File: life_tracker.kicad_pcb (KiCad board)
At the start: 2 copper layers, 52 x 78 mm, 16 parts, among them J1 TACTILE-NAV-SWITCH, U1 WeMos_D1_mini, U2 I2C_128x64_OLED, U3 AS1115-BSST, U4 PTS526-tactile-button, U5 PTS526-tactile-button

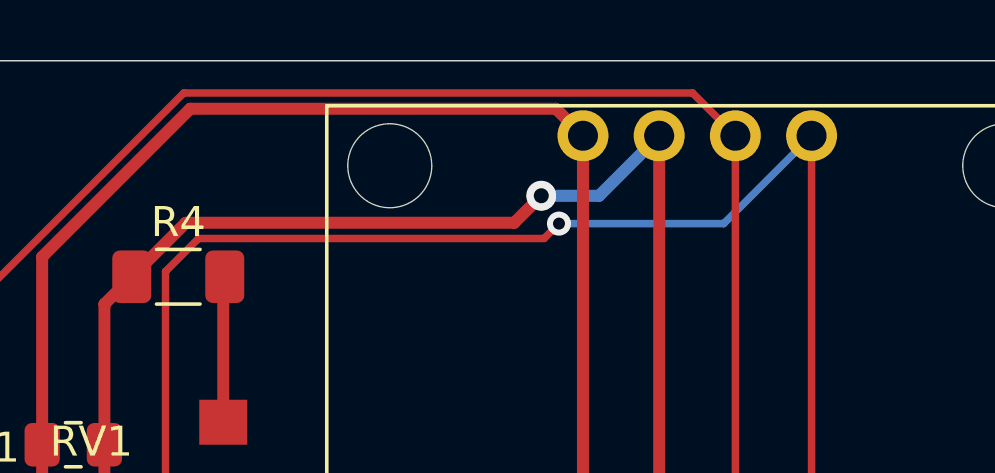
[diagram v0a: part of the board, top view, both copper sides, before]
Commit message: Fix swapped I2C connection.
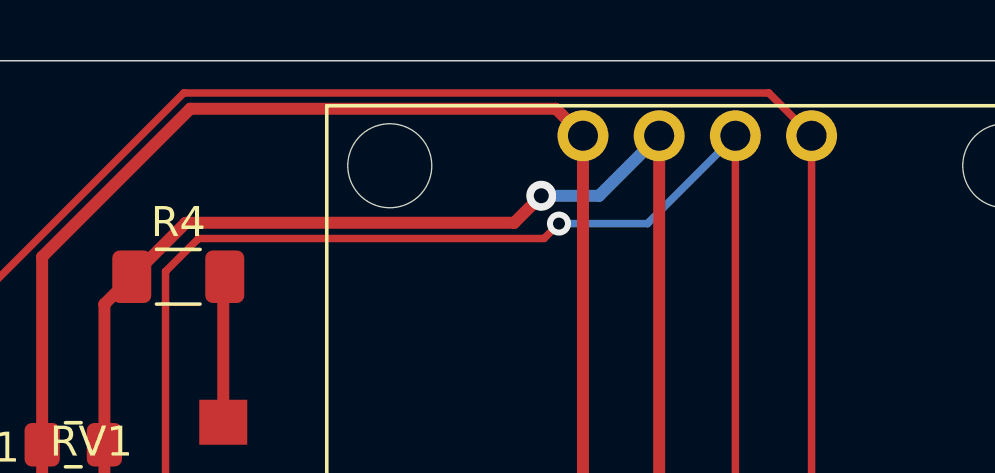
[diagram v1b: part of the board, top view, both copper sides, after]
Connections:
- U1 pad 10: GND -> Net-(U1-Pad10)
- U3 pad 1: Net-(R1-Pad2) -> Net-(R2-Pad2)
- U3 pad 14: Net-(R2-Pad2) -> Net-(R1-Pad2)
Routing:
- net Net-(R2-Pad2): track 156.2 -> 149.7 mm, vias 4 -> 1
- net Net-(R1-Pad2): track 144.9 -> 151.5 mm, vias 1 -> 4

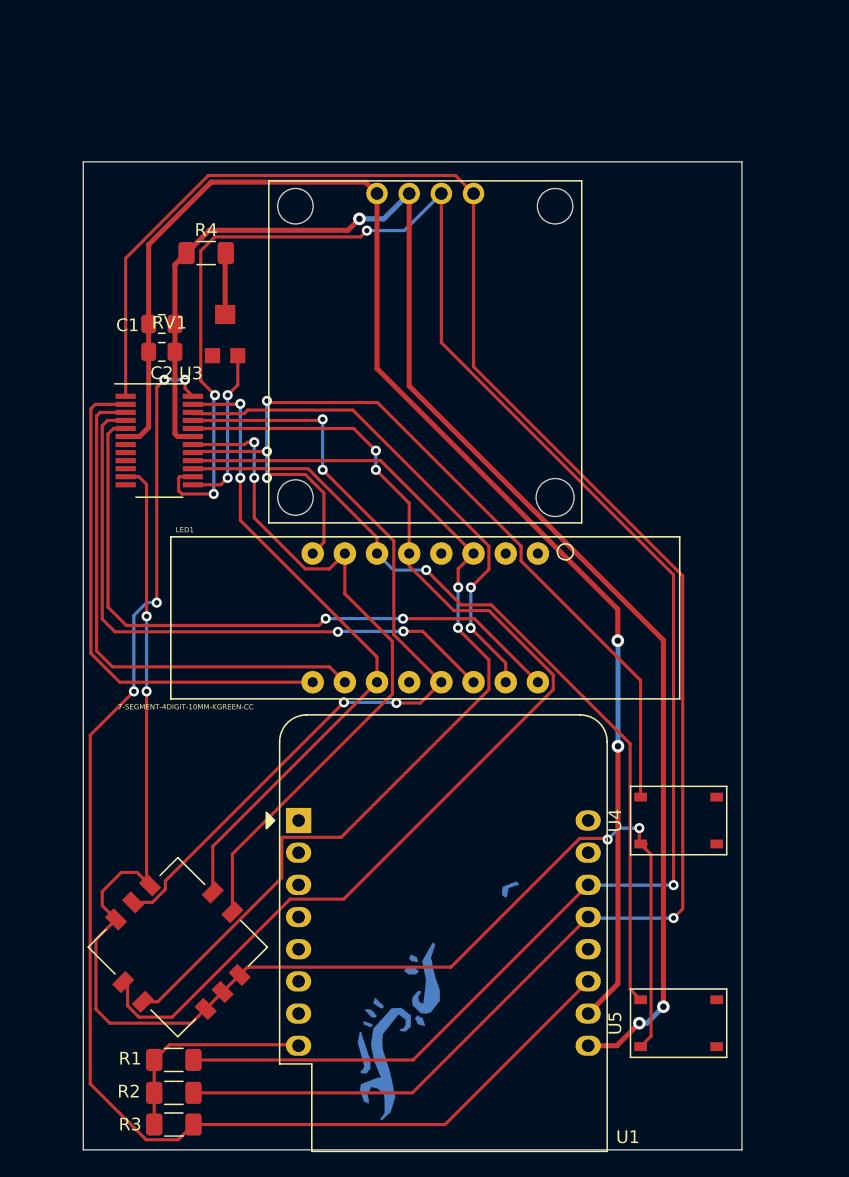
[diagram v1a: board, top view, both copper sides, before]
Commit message: Added footprints for new buttons and redid layout for bigger board, and OLED on top of D1.
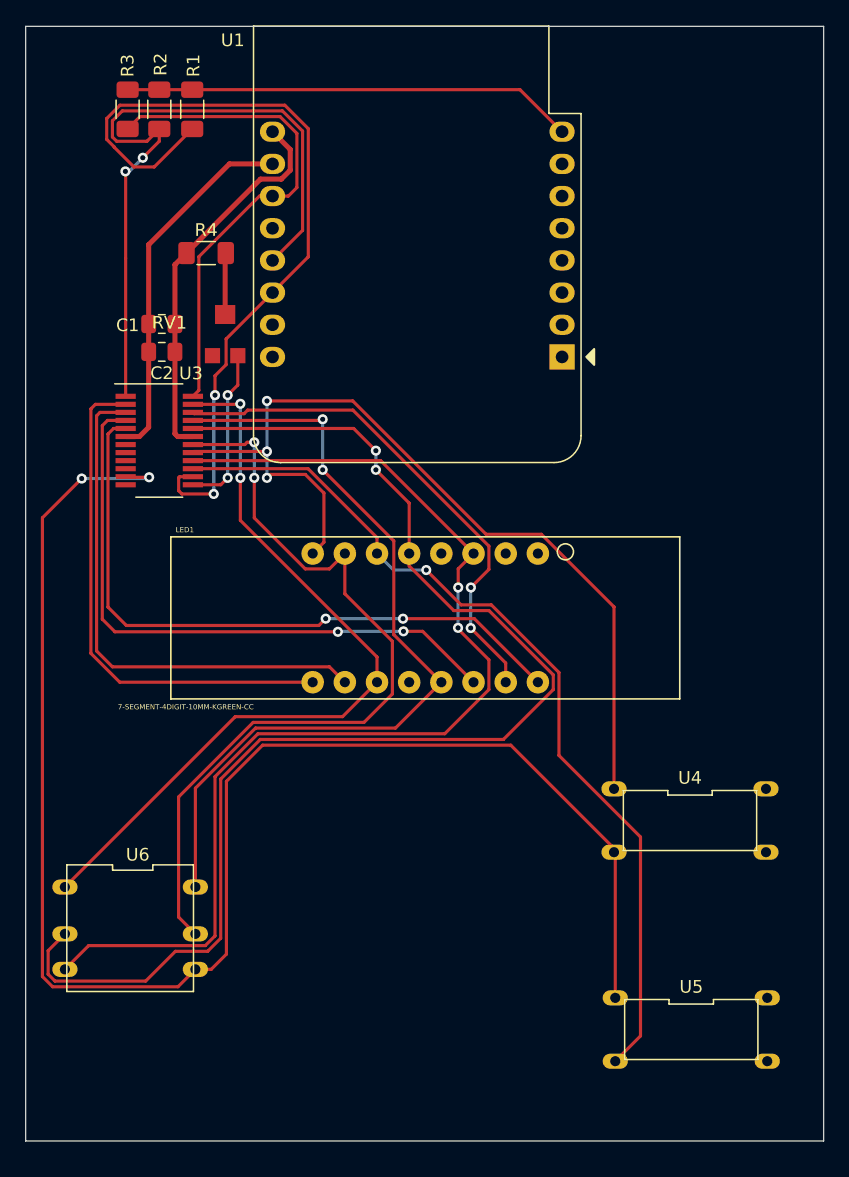
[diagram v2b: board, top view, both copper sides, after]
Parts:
- removed J1: TACTILE-NAV-SWITCH, MyFootprints:JS1300AQ
- removed U2: I2C_128x64_OLED, MyFootprints:I2C_128x64_OLED
- removed svg2mod: G***, MyFootprints:squirrel2
- removed svg2mod: G***, MyFootprints:plains_walker
- added U6: TACTILE-NAV-STICK-DIP, MyFootprints:TACTILE-NAV-STICK-DIP, F.Cu at (103.7, 110.5)
- U4, U5: footprint MyFootprints:pts526-tactile-button -> MyFootprints:TACTILE-DIP-BUTTON
- moved R3 80.2 mm to (103.5, 45.9), turned to 270 degrees
- moved R2 77.7 mm to (106.0, 45.9), turned to 270 degrees
- moved R1 75.1 mm to (108.6, 45.9), turned to 270 degrees
- moved U1 42.1 mm to (137.8, 65.4), turned to 180 degrees
- moved U5 1.12 mm to (148.0, 118.5), turned to 270 degrees
- moved U4 0.90 mm to (147.9, 102.0), turned to 270 degrees
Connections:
- U1 pad 10: Net-(U1-Pad10) -> GND
- U3 pad 11: Net-(J1-Pad10) -> Net-(U3-Pad11)
- U4 pad 3: Net-(J1-Pad10) -> Net-(U3-Pad11)
- U5 pad 1: Net-(LED1-Pad14) -> Net-(U3-Pad11)
- U5 pad 3: Net-(J1-Pad10) -> Net-(LED1-Pad14)
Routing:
- net Net-(U3-Pad11): track 0.00 -> 124.7 mm, vias 0 -> 2
- net Net-(J1-Pad10): track 117.1 -> 0.00 mm, vias 4 -> 0
- net Net-(R2-Pad2): track 149.7 -> 55.1 mm, vias 1 -> 2
- net Net-(R1-Pad2): track 151.5 -> 64.7 mm, vias 4 -> 2
- net +5V: track 115.4 -> 30.7 mm, vias 3 -> 0
- net GND: track 110.6 -> 29.0 mm, vias 2 -> 0
- net Net-(R3-Pad2): track 108.0 -> 40.5 mm, vias 4 -> 0
- net Net-(R1-Pad1): track 17.0 -> 35.7 mm
- net Net-(LED1-Pad13): track 88.9 -> 102.2 mm
- net Net-(LED1-Pad11): track 76.8 -> 87.4 mm
- net Net-(LED1-Pad3): track 52.2 -> 61.6 mm
- net Net-(LED1-Pad15): track 55.4 -> 64.5 mm
- net Net-(LED1-Pad14): track 64.8 -> 70.5 mm
- net Net-(LED1-Pad5): track 66.9 -> 65.6 mm, vias 4 -> 2
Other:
- board size 52 x 78 mm -> 63 x 88 mm

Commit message: Added art for second revision.
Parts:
- added svg2mod: G***, MyFootprints:squirrel2, B.Cu at (137.9, 40.0)
- added svg2mod: G***, MyFootprints:lotus, F.Cu at (157.9, 44.1)
- added svg2mod: G***, MyFootprints:plains_walker_back_simp2, F.Cu at (114.5, 93.0)
